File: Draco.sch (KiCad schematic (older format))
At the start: 55 parts, among them J1 Conn_01x03, J10 Conn_01x03, J11 Conn_01x06, J12 Conn_02x05_Odd_Even, J13 Conn_01x04, J14 Conn_01x01, J15 Micro_SD_Card, J2 Conn_01x03, J20 Conn_01x04, J3 Conn_01x03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

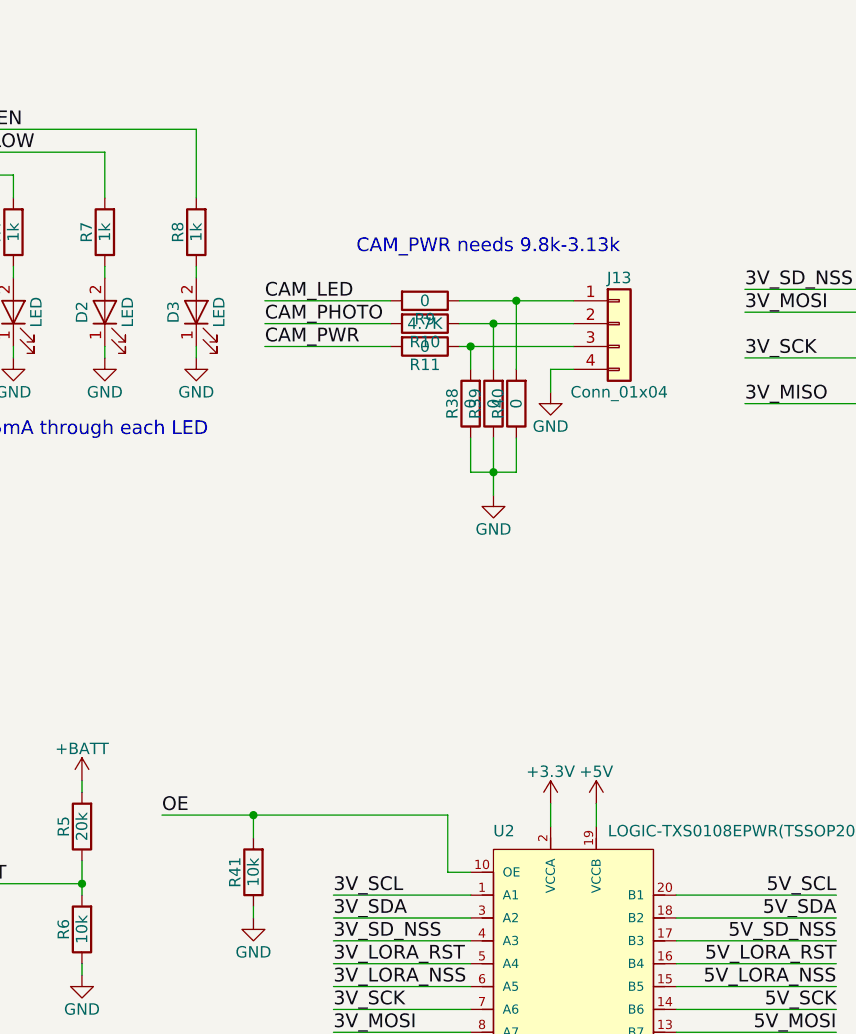
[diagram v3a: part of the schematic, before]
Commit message: Added camera power
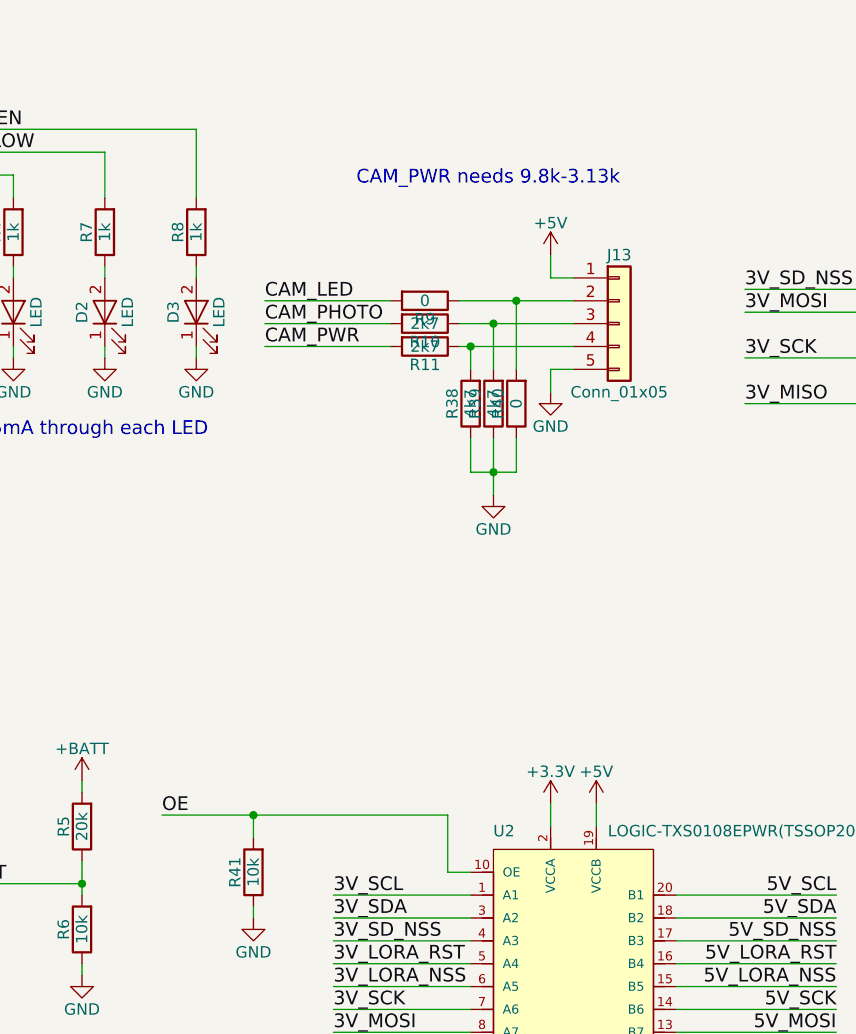
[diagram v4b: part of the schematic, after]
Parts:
- removed J13: Conn_01x04, Connectors_JST:JST_XH_B04B-XH-A_04x2.50mm_Straight, symbol Conn_01x04
- added J13: Conn_01x05, Connectors_JST:JST_XH_B05B-XH-A_05x2.50mm_Straight, symbol Conn_01x05
- R10: value 4.7K -> 2k7
- R11: value 0 -> 2k7
- R38, R39: value 0 -> 4k7
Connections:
- net +5V: now also J13.1 (Pin_1)
- net GND: now also J13.5 (Pin_5)
- net at R40.2, R9.1: now also J13.2 (Pin_2)
- net at R10.1, R39.2: now also J13.3 (Pin_3)
- net at R11.1, R38.2: now also J13.4 (Pin_4)
